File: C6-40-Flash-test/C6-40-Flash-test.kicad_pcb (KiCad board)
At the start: 4 copper layers, 19.7 x 31.1 mm, 22 parts, among them IC1 W25Q80DVSSIG, J1 USB_C_Receptacle_USB2.0, J2 Conn_01x07, J3 Conn_01x07, SW1 SW_Push_Dual, U2 ESP32-C6, U3 MCP1700-3302E_SOT23, X1 Crystal 40 Mhz 10ppm

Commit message: Make antenna better (Is a shoelace)
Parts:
- added IC2: W25Q128JVSIQ, footprints:SOIC127P790X216-8N, B.Cu at (144.2, 109.7)
- moved L2 78.8 mm to (134.3, 103.1), turned to 45 degrees
- moved C1 78.5 mm to (137.8, 107.8)
- moved C4 78.5 mm to (137.9, 91.2)
- moved C5 78.5 mm to (138.2, 97.5)
- moved C6 78.5 mm to (137.9, 101.5)
- moved C7 78.5 mm to (137.9, 104.6)
- moved IC1 78.5 mm to (146.5, 109.3)
- moved J1 78.5 mm to (142.2, 84.0)
- moved J2 78.5 mm to (134.2, 84.5)
- moved J3 78.5 mm to (150.1, 84.5)
- moved L1 78.5 mm to (137.9, 103.1)
- moved R1 78.5 mm to (144.8, 90.1)
- moved R6 78.5 mm to (140.0, 104.4)
- moved SW1 78.5 mm to (135.9, 110.5)
- moved U2 78.5 mm to (143.7, 99.9)
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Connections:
- J3 pad 4: unconnected-(J3-Pin_4-Pad4) -> SPIVDD
- J3 pad 5: unconnected-(J3-Pin_5-Pad5) -> RX
- J3 pad 6: unconnected-(J3-Pin_6-Pad6) -> TX
- U2 pad 29: unconnected-(U2-U0TXD/GPIO16/FSPICS0-Pad29) -> TX
- U2 pad 30: unconnected-(U2-U0RXD/GPIO17/FSPICS1-Pad30) -> RX
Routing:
- net SPIVDD: track 11.8 -> 25.5 mm
- net SPICS0: track 9.03 -> 19.1 mm
- net RX: track 0.00 -> 7.47 mm, vias 0 -> 1
- net TX: track 0.00 -> 7.40 mm, vias 0 -> 1
- net SPI_D1: track 13.6 -> 21.0 mm
- net SPI_D3: track 16.4 -> 22.6 mm
- net SPICLK: track 18.8 -> 22.4 mm
- net GND: track 22.6 -> 24.8 mm, vias 12 -> 23
- net IO5: track 20.2 -> 18.4 mm, vias 0 -> 1
- net SPI_D0: track 20.6 -> 22.0 mm
- net SPI_D2: track 16.1 -> 17.2 mm
- net IO4: track 17.1 -> 16.1 mm
- net unconnected-(L2-Pad1): track 11.3 -> 10.7 mm
- net IO6: track 18.5 -> 18.0 mm
- added copper zone on F.Cu, net GND
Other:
- board text added: "0"
- board text added: "1"
- board text added: "16"
- board text added: "17"
- board text added: "2"
- board text added: "3"
- board text added: "3V3"
- board text added: "4"
- board text added: "5V"
- board text added: "6"
- board text added: "7"
- board text added: "FLASH"
- board text added: "GND"
- board text added: "SPI"
- board text added: "Vdd"

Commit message: C6 test new Flash
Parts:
- IC1: value W25Q80DVSSIG -> AT25SF041-XMHD-T; footprint foot_main:SOIC127P790X216-8N-FLASH -> footprints:SOP65P640X120-8N_flash
- moved IC1 0.94 mm to (147.2, 108.7)
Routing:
- net SPICS0: track 19.1 -> 20.3 mm
- net SPI_D2: track 17.2 -> 18.4 mm
- net SPI_D1: track 21.0 -> 21.8 mm
- net SPI_D0: track 22.0 -> 21.4 mm

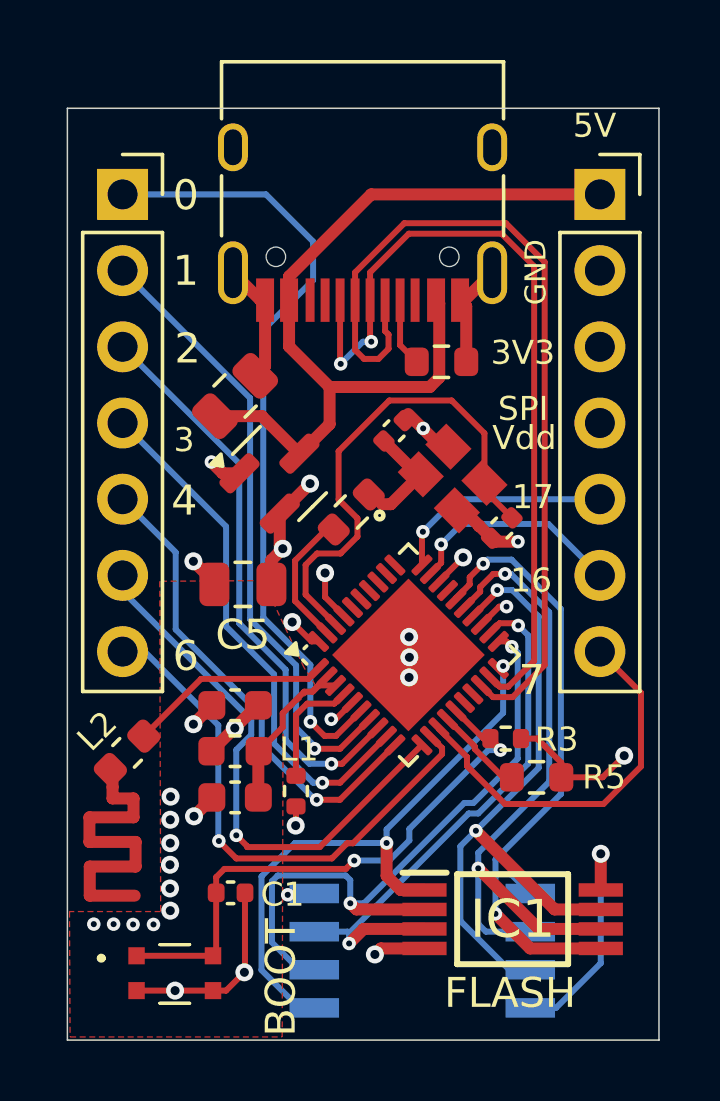
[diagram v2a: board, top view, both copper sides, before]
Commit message: Test with external flash
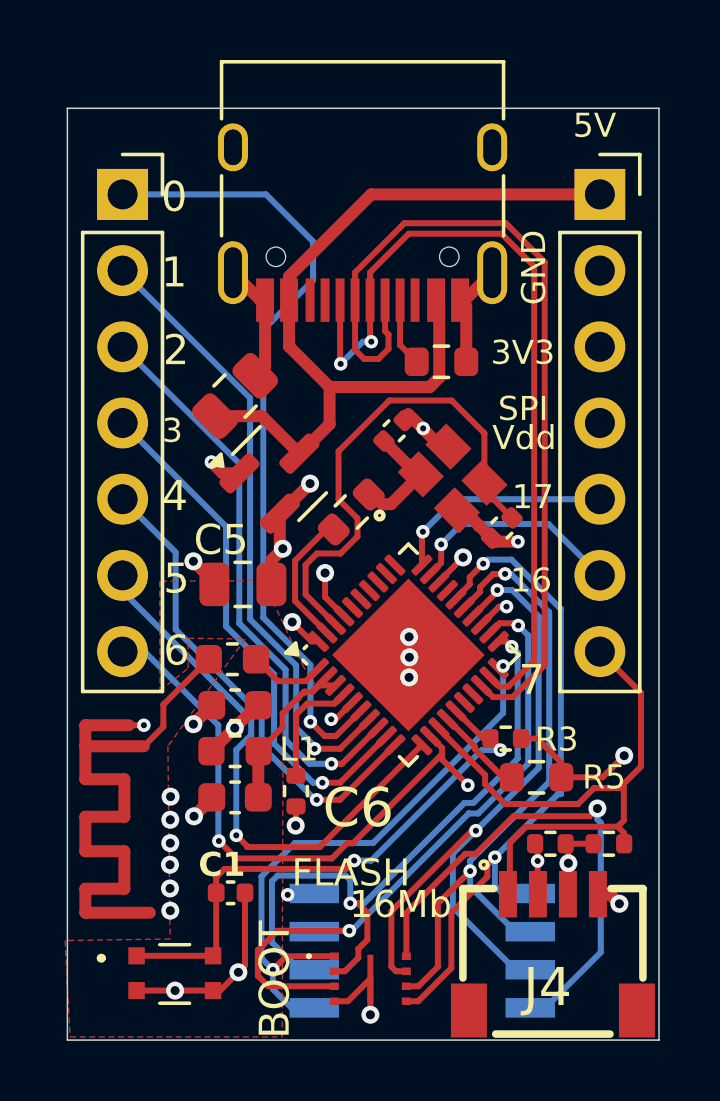
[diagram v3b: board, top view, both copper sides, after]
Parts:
- added J4: SM04B-SRSS-TB_LF__SN_, foot_main:QWIIC_SM04B-SRSS-TB_LFSN_, F.Cu at (145.5, 112.5)
- added R2: 10k, Resistor_SMD:R_0402_1005Metric, F.Cu at (150.4, 106.2)
- added R7: 10k, Resistor_SMD:R_0402_1005Metric, F.Cu at (148.4, 106.2)
- IC1: value AT25SF041-XMHD-T -> MX25R1635FZUIL0_TR; footprint footprints:SOP65P640X120-8N_flash -> footprints:MX25R1635FZUIL0TR
- moved IC1 5.14 mm to (142.4, 110.7)
- moved L2 4.70 mm to (137.8, 100.0), turned to 0 degrees
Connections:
- L2 pad 1: unconnected-(L2-Pad1) -> GND
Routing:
- net GND: track 25.0 -> 48.1 mm, vias 23 -> 21
- net unconnected-(L2-Pad1): track 10.7 -> 0.00 mm
- net SPIVDD: track 25.8 -> 33.7 mm
- net IO7: track 12.9 -> 20.6 mm
- net IO6: track 18.0 -> 24.6 mm, vias 1 -> 3
- net Net-(U2-ANT): track 6.76 -> 2.56 mm
- net SPI_D2: track 18.4 -> 22.2 mm
- net +3V3: track 20.4 -> 23.1 mm, vias 9 -> 10
- net SPI_D0: track 21.4 -> 22.6 mm
- net SPI_D3: track 22.4 -> 23.6 mm
- net SPI_D1: track 21.8 -> 22.6 mm
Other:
- board text added: "16Mb"
- board text added: "2nd Flash"
- board text added: "5"
- board text added: "C6"
